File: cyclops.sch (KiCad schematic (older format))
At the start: 138 parts, among them J1 USB_mini_micro_B, K1 ESC, K10 KEYSW, K11 KEYSW, K12 KEYSW, K13 KEYSW, K14 backspace, K15 tab, K16 KEYSW, K17 KEYSW, K18 KEYSW, K19 KEYSW, K2 1, K20 KEYSW, K21 KEYSW, K22 KEYSW, K23 KEYSW, K24 KEYSW, K25 KEYSW, K26 KEYSW, K27 KEYSW, K28 Lock, K29 KEYSW, K3 KEYSW, K30 KEYSW, K31 KEYSW, K32 KEYSW, K33 KEYSW, K34 KEYSW, K35 KEYSW, K36 KEYSW, K37 KEYSW, K38 KEYSW, K39 KEYSW, K4 KEYSW, K40 KEYSW, K41 Shift, K42 KEYSW, K43 KEYSW, K44 KEYSW, K45 KEYSW, K46 KEYSW, K47 KEYSW, K48 KEYSW, K49 KEYSW, K5 KEYSW, K50 KEYSW, K51 KEYSW, K52 KEYSW, K53 Shift, K54 Ctrl, K55 alt, K56 opt, K57 space, K58 cmd, K59 alt, K6 KEYSW, K60 ctrl, K61 enter, K7 KEYSW, K8 KEYSW, K9 KEYSW, SW1 SW_Push, U1 ATMEGA32U2, X1 XTAL_GND

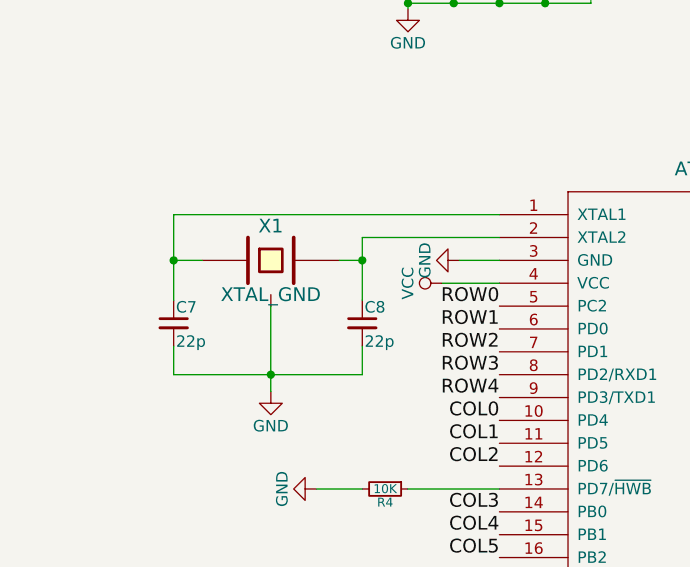
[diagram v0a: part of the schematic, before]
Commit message: PCB layout complete
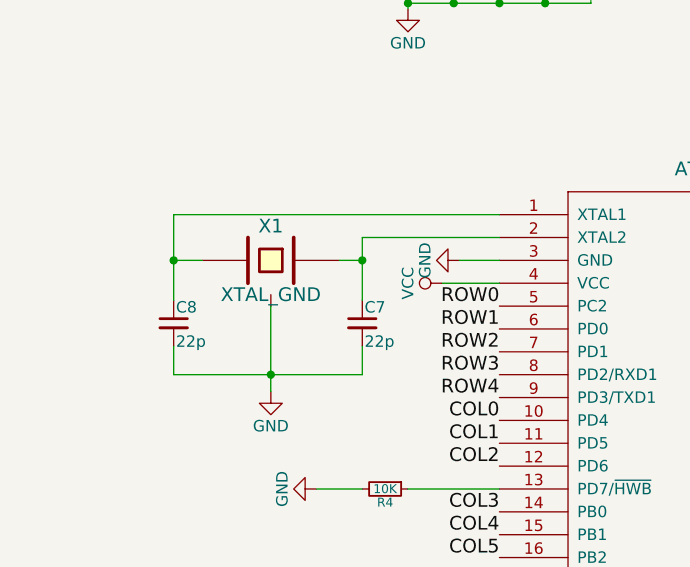
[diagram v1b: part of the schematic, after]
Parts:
- X1: footprint Crystals:Crystal_SMD_0603-4pin_6.0x3.5mm_HandSoldering -> Crystals:Crystal_SMD_SeikoEpson_FA238-4pin_3.2x2.5mm_HandSoldering
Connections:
- net at C7.1, X1.1: now also U1.2 (XTAL2); no longer U1.1 (XTAL1)
- net at C8.1, X1.2: now also U1.1 (XTAL1); no longer U1.2 (XTAL2)
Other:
- moved on the sheet: C7, C8
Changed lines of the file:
@@
 L C_Small C7
 U 1 1 5A32767B
-P 1425 3050
-F 0 "C7" H 1435 3120 50  0000 L CNN
-F 1 "22p" H 1435 2970 50  0000 L CNN
-F 2 "Capacitors_SMD:C_0805_HandSoldering" H 1425 3050 50  0001 C CNN
-F 3 "" H 1425 3050 50  0001 C CNN
-	1    1425 3050
+P 2250 3050
+F 0 "C7" H 2260 3120 50  0000 L CNN
+F 1 "22p" H 2260 2970 50  0000 L CNN
+F 2 "Capacitors_SMD:C_0805_HandSoldering" H 2250 3050 50  0001 C CNN
+F 3 "" H 2250 3050 50  0001 C CNN
+	1    2250 3050
 	1    0    0    -1
 $EndComp
@@
 L C_Small C8
 U 1 1 5A3276EA
-P 2250 3050
-F 0 "C8" H 2260 3120 50  0000 L CNN
-F 1 "22p" H 2260 2970 50  0000 L CNN
-F 2 "Capacitors_SMD:C_0805_HandSoldering" H 2250 3050 50  0001 C CNN
-F 3 "" H 2250 3050 50  0001 C CNN
-	1    2250 3050
+P 1425 3050
+F 0 "C8" H 1435 3120 50  0000 L CNN
+F 1 "22p" H 1435 2970 50  0000 L CNN
+F 2 "Capacitors_SMD:C_0805_HandSoldering" H 1425 3050 50  0001 C CNN
+F 3 "" H 1425 3050 50  0001 C CNN
+	1    1425 3050
 	1    0    0    -1
 $EndComp
@@
 F 0 "X1" H 1850 2925 60  0000 C CNN
 F 1 "XTAL_GND" H 1850 2625 60  0000 C CNN
-F 2 "Crystals:Crystal_SMD_0603-4pin_6.0x3.5mm_HandSoldering" H 1850 2775 60  0001 C CNN
+F 2 "Crystals:Crystal_SMD_SeikoEpson_FA238-4pin_3.2x2.5mm_HandSoldering" H 1850 2775 60  0001 C CNN
 F 3 "" H 1850 2775 60  0000 C CNN
 	1    1850 2775
-	1    0    0    -1
+	-1   0    0    -1
 $EndComp
 Wire Wire Line

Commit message: pcb complete
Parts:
- J1: footprint keyboard_parts:USB_miniB_hirose_5ST_hand -> keyboard_parts:USB_miniB_hirose_5S8
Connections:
- net COL0: now also U1.8 (PD2/RXD1); no longer U1.10 (PD4)
- net COL1: now also U1.7 (PD1); no longer U1.11 (PD5)
- net COL10: now also U1.20 (PB6); no longer U1.21 (PB7)
- net COL11: now also U1.21 (PB7); no longer U1.20 (PB6)
- net COL12: now also U1.23 (PC6); no longer U1.19 (PB5)
- net COL13: now also U1.22 (PC7); no longer U1.18 (PB4)
- net COL2: now also U1.9 (PD3/TXD1); no longer U1.12 (PD6)
- net COL3: now also U1.10 (PD4); no longer U1.14 (PB0)
- net COL4: now also U1.14 (PB0); no longer U1.15 (PB1)
- net COL5: now also U1.15 (PB1); no longer U1.16 (PB2)
- net COL6: now also U1.16 (PB2); no longer U1.26 (PC4)
- net COL7: now also U1.17 (PB3); no longer U1.25 (PC5)
- net COL8: now also U1.18 (PB4); no longer U1.23 (PC6)
- net COL9: now also U1.19 (PB5); no longer U1.22 (PC7)
- net GND: now also C6.2, J1.5 (GND), J1.6 (SHIELD), U1.28 (UGND)
- net ROW0: now also U1.6 (PD0); no longer U1.5 (PC2)
- net ROW1: now also D22.1 (K), U1.5 (PC2); no longer U1.6 (PD0)
- net ROW2: now also U1.11 (PD5); no longer U1.7 (PD1)
- net ROW3: now also U1.12 (PD6); no longer U1.8 (PD2/RXD1)
- net ROW4: now also U1.26 (PC4); no longer U1.9 (PD3/TXD1)
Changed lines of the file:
@@
 F 0 "J1" H 6225 2675 60  0000 C CNN
 F 1 "USB_mini_micro_B" H 6475 2975 60  0001 C CNN
-F 2 "keyboard_parts:USB_miniB_hirose_5ST_hand" H 6575 2725 60  0001 C CNN
+F 2 "keyboard_parts:USB_miniB_hirose_5S8" H 6575 2725 60  0001 C CNN
 F 3 "" H 6575 2725 60  0000 C CNN
 	1    6625 2725
@@
 	5250 2575 5250 2675
 Connection ~ 5250 2675
+Text Label 2850 3075 2    60   ~ 0
+ROW0
 Text Label 2850 2975 2    60   ~ 0
-ROW0
-Text Label 2850 3075 2    60   ~ 0
 ROW1
+Text Label 2850 3575 2    60   ~ 0
+ROW2
+Text Label 2850 3675 2    60   ~ 0
+ROW3
+Text Label 5000 3175 0    60   ~ 0
+ROW4
+Text Label 2850 3275 2    60   ~ 0
+COL0
 Text Label 2850 3175 2    60   ~ 0
-ROW2
-Text Label 2850 3275 2    60   ~ 0
-ROW3
+COL1
 Text Label 2850 3375 2    60   ~ 0
-ROW4
+COL2
 Text Label 2850 3475 2    60   ~ 0
-COL0
-Text Label 2850 3575 2    60   ~ 0
-COL1
-Text Label 2850 3675 2    60   ~ 0
-COL2
+COL3
 Text Label 2850 3875 2    60   ~ 0
-COL3
+COL4
 Text Label 2850 3975 2    60   ~ 0
-COL4
+COL5
 Text Label 2850 4075 2    60   ~ 0
-COL5
-Text Label 5000 3175 0    60   ~ 0
 COL6
-Text Label 5000 3275 0    60   ~ 0
+Text Label 5000 4075 0    60   ~ 0
 COL7
+Text Label 5000 3975 0    60   ~ 0
+COL8
+Text Label 5000 3875 0    60   ~ 0
+COL9
+Text Label 5000 3775 0    60   ~ 0
+COL10
+Text Label 5000 3675 0    60   ~ 0
+COL11
 Text Label 5000 3475 0    60   ~ 0
-COL8
+COL12
 Text Label 5000 3575 0    60   ~ 0
-COL9
-Text Label 5000 3675 0    60   ~ 0
-COL10
-Text Label 5000 3775 0    60   ~ 0
-COL11
-Text Label 5000 3875 0    60   ~ 0
-COL12
-Text Label 5000 3975 0    60   ~ 0
 COL13
-NoConn ~ 5000 4075
+NoConn ~ 5000 3275
+Connection ~ 9300 6650
+Connection ~ 4825 4325
+$Comp
+L GND #PWR010
+U 1 1 5A4D63E6
+P 6100 2975
+F 0 "#PWR010" H 6100 2725 50  0001 C CNN
+F 1 "GND" H 6100 2825 50  0000 C CNN
+F 2 "" H 6100 2975 50  0001 C CNN
+F 3 "" H 6100 2975 50  0001 C CNN
+	1    6100 2975
+	1    0    0    -1
+$EndComp
+Connection ~ 6100 2975
 $EndSCHEMATC

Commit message: pcb minor fixes
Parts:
- removed C3, C4: 0.1u, Capacitors_SMD:C_0805_HandSoldering, symbol C_Small
- renumbered C5 to C3, C6 to C4, C7 to C5, C8 to C6
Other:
- moved on the sheet: C3
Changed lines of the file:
@@
 $EndDescr
 $Comp
-L C_Small C7
+L C_Small C5
 U 1 1 5A32767B
 P 2250 3050
-F 0 "C7" H 2260 3120 50  0000 L CNN
+F 0 "C5" H 2260 3120 50  0000 L CNN
 F 1 "22p" H 2260 2970 50  0000 L CNN
 F 2 "Capacitors_SMD:C_0805_HandSoldering" H 2250 3050 50  0001 C CNN
@@
 $EndComp
 $Comp
-L C_Small C8
+L C_Small C6
 U 1 1 5A3276EA
 P 1425 3050
-F 0 "C8" H 1435 3120 50  0000 L CNN
+F 0 "C6" H 1435 3120 50  0000 L CNN
 F 1 "22p" H 1435 2970 50  0000 L CNN
 F 2 "Capacitors_SMD:C_0805_HandSoldering" H 1425 3050 50  0001 C CNN
@@
 Connection ~ 1850 3275
 $Comp
-L GND #PWR01
+L GND #PWR7
 U 1 1 5A32776A
 P 1850 3350
-F 0 "#PWR01" H 1850 3100 50  0001 C CNN
+F 0 "#PWR7" H 1850 3100 50  0001 C CNN
 F 1 "GND" H 1850 3200 50  0000 C CNN
 F 2 "" H 1850 3350 50  0001 C CNN
@@
 $Comp
 L C_Small C3
-U 1 1 5A328440
+U 1 1 5A3284C2
 P 2850 1500
 F 0 "C3" H 2860 1570 50  0000 L CNN
-F 1 "0.1u" H 2860 1420 50  0000 L CNN
+F 1 "4.7u" H 2860 1420 50  0000 L CNN
 F 2 "Capacitors_SMD:C_0805_HandSoldering" H 2850 1500 50  0001 C CNN
 F 3 "" H 2850 1500 50  0001 C CNN
@@
 $EndComp
 $Comp
-L C_Small C4
-U 1 1 5A32846F
-P 3050 1500
-F 0 "C4" H 3060 1570 50  0000 L CNN
-F 1 "0.1u" H 3060 1420 50  0000 L CNN
-F 2 "Capacitors_SMD:C_0805_HandSoldering" H 3050 1500 50  0001 C CNN
-F 3 "" H 3050 1500 50  0001 C CNN
-	1    3050 1500
-	1    0    0    -1
-$EndComp
-$Comp
-L C_Small C5
-U 1 1 5A3284C2
-P 3250 1500
-F 0 "C5" H 3260 1570 50  0000 L CNN
-F 1 "4.7u" H 3260 1420 50  0000 L CNN
-F 2 "Capacitors_SMD:C_0805_HandSoldering" H 3250 1500 50  0001 C CNN
-F 3 "" H 3250 1500 50  0001 C CNN
-	1    3250 1500
-	1    0    0    -1
-$EndComp
-$Comp
-L GND #PWR02
+L GND #PWR2
 U 1 1 5A328570
 P 2450 1675
-F 0 "#PWR02" H 2450 1425 50  0001 C CNN
+F 0 "#PWR2" H 2450 1425 50  0001 C CNN
 F 1 "GND" H 2450 1525 50  0000 C CNN
 F 2 "" H 2450 1675 50  0001 C CNN
@@
 $EndComp
 $Comp
-L VCC #PWR03
+L VCC #PWR1
 U 1 1 5A328596
 P 2450 1325
-F 0 "#PWR03" H 2450 1175 50  0001 C CNN
+F 0 "#PWR1" H 2450 1175 50  0001 C CNN
 F 1 "VCC" H 2450 1475 50  0000 C CNN
 F 2 "" H 2450 1325 50  0001 C CNN
@@
 Wire Wire Line
 	2450 1600 2450 1675
-Wire Wire Line
-	2450 1650 3250 1650
-Wire Wire Line
-	3250 1650 3250 1600
 Connection ~ 2450 1650
 Wire Wire Line
 	2450 1325 2450 1400
 Wire Wire Line
-	2450 1350 3250 1350
-Wire Wire Line
-	3250 1350 3250 1400
+	2450 1350 2850 1350
 Connection ~ 2450 1350
 Wire Wire Line
@@
 Connection ~ 2650 1350
 Wire Wire Line
-	2850 1400 2850 1350
-Connection ~ 2850 1350
+	2850 1350 2850 1400
 Wire Wire Line
 	2650 1600 2650 1650
@@
 Wire Wire Line
 	2850 1600 2850 1650
-Connection ~ 2850 1650
-Wire Wire Line
-	3050 1600 3050 1650
-Connection ~ 3050 1650
-Wire Wire Line
-	3050 1400 3050 1350
-Connection ~ 3050 1350
 $Comp
 L SW_Push SW1
@@
 	5000 3375 5450 3375
 $Comp
-L GND #PWR04
+L GND #PWR8
 U 1 1 5A328DC7
 P 5975 3375
-F 0 "#PWR04" H 5975 3125 50  0001 C CNN
+F 0 "#PWR8" H 5975 3125 50  0001 C CNN
 F 1 "GND" H 5975 3225 50  0000 C CNN
 F 2 "" H 5975 3375 50  0001 C CNN
@@
 $EndComp
 $Comp
-L VCC #PWR05
+L VCC #PWR9
 U 1 1 5A328DEF
 P 5900 3550
-F 0 "#PWR05" H 5900 3400 50  0001 C CNN
+F 0 "#PWR9" H 5900 3400 50  0001 C CNN
 F 1 "VCC" H 5900 3700 50  0000 C CNN
 F 2 "" H 5900 3550 50  0001 C CNN
@@
 	5975 3375 5850 3375
 $Comp
-L GND #PWR06
+L GND #PWR10
 U 1 1 5A328FCC
 P 2050 3775
-F 0 "#PWR06" H 2050 3525 50  0001 C CNN
+F 0 "#PWR10" H 2050 3525 50  0001 C CNN
 F 1 "GND" H 2050 3625 50  0000 C CNN
 F 2 "" H 2050 3775 50  0001 C CNN
@@
 	6200 2675 5000 2675
 $Comp
-L VCC #PWR07
+L VCC #PWR3
 U 1 1 5A329DCE
 P 6400 2550
-F 0 "#PWR07" H 6400 2400 50  0001 C CNN
+F 0 "#PWR3" H 6400 2400 50  0001 C CNN
 F 1 "VCC" H 6400 2700 50  0000 C CNN
 F 2 "" H 6400 2550 50  0001 C CNN
@@
 	5425 2975 5425 3075
 $Comp
-L C_Small C6
+L C_Small C4
 U 1 1 5A329E92
 P 5200 3075
-F 0 "C6" V 5224 3110 35  0000 L CNN
+F 0 "C4" V 5224 3110 35  0000 L CNN
 F 1 "1u" V 5224 3036 35  0000 R CNN
 F 2 "Capacitors_SMD:C_0805_HandSoldering" H 5200 3075 50  0001 C CNN
@@
 	6300 2675 6300 2775
 $Comp
-L VCC #PWR08
+L VCC #PWR5
 U 1 1 5A39CBC6
 P 2600 2875
-F 0 "#PWR08" H 2600 2725 50  0001 C CNN
+F 0 "#PWR5" H 2600 2725 50  0001 C CNN
 F 1 "VCC" H 2600 3025 50  0000 C CNN
 F 2 "" H 2600 2875 50  0001 C CNN
@@
 $EndComp
 $Comp
-L GND #PWR09
+L GND #PWR4
 U 1 1 5A39CCEE
 P 2675 2775
-F 0 "#PWR09" H 2675 2525 50  0001 C CNN
+F 0 "#PWR4" H 2675 2525 50  0001 C CNN
 F 1 "GND" H 2675 2625 50  0000 C CNN
 F 2 "" H 2675 2775 50  0001 C CNN
@@
 Connection ~ 4825 4325
 $Comp
-L GND #PWR010
+L GND #PWR6
 U 1 1 5A4D63E6
 P 6100 2975
-F 0 "#PWR010" H 6100 2725 50  0001 C CNN
+F 0 "#PWR6" H 6100 2725 50  0001 C CNN
 F 1 "GND" H 6100 2825 50  0000 C CNN
 F 2 "" H 6100 2975 50  0001 C CNN
@@
 $EndComp
 Connection ~ 6100 2975
+Wire Wire Line
+	2850 1650 2450 1650
 $EndSCHEMATC

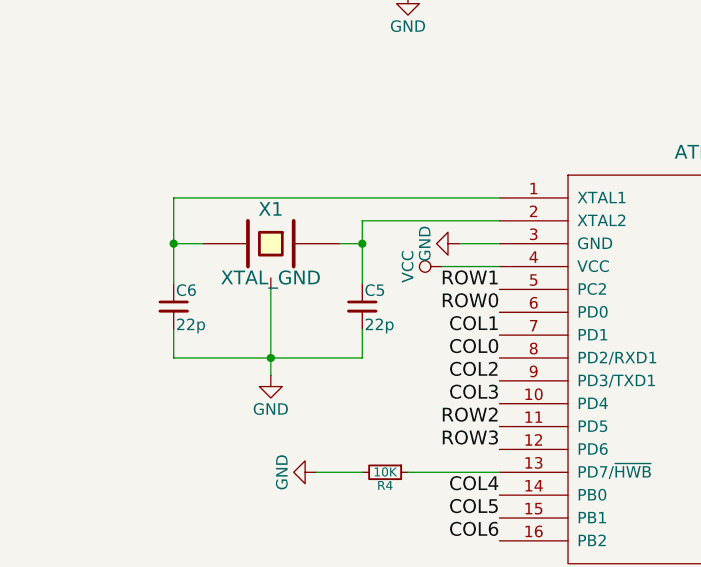
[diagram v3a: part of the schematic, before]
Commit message: Correct the crystal
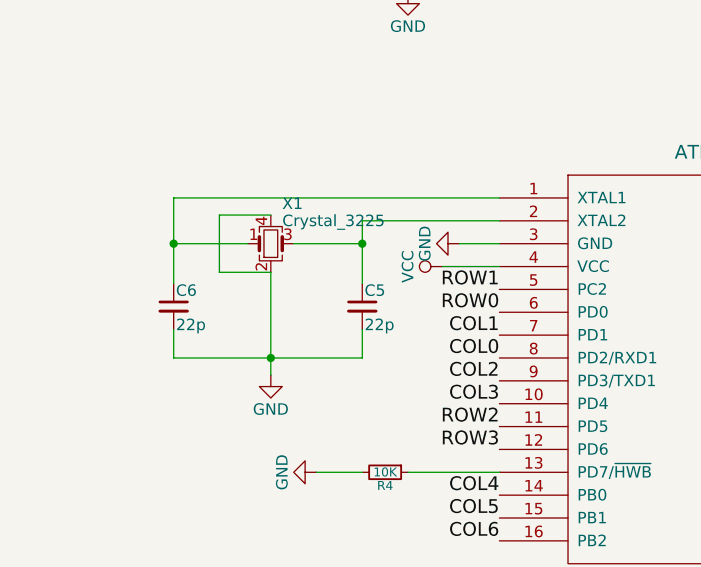
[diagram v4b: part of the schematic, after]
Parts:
- removed X1: XTAL_GND, Crystals:Crystal_SMD_SeikoEpson_FA238-4pin_3.2x2.5mm_HandSoldering, symbol XTAL_GND
- added X1: Crystal_3225, Crystals:Crystal_SMD_3225-4pin_3.2x2.5mm_HandSoldering, symbol Crystal_GND24_Small
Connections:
- net GND: now also X1.2, X1.4
- net at C5.1, U1.2 (XTAL2): now also X1.3
- net at C6.1, U1.1 (XTAL1): now also X1.1
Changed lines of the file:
@@
 LIBS:contrib
 LIBS:valves
-LIBS:cartel
-LIBS:keyboard_parts
-LIBS:mkl27z256vfm4
-LIBS:ws2812b
 LIBS:cyclops-cache
 EELAYER 25 0
@@
 $EndComp
 Wire Wire Line
-	2150 2775 2250 2775
+	1950 2775 2250 2775
 Wire Wire Line
 	2250 2675 2250 2950
@@
 	2250 3275 2250 3150
 Wire Wire Line
-	1850 2975 1850 3350
+	1850 2900 1850 3350
 Connection ~ 1850 3275
 $Comp
@@
 	1    0    0    -1
 $EndComp
-$Comp
-L XTAL_GND X1
-U 1 1 5A327837
-P 1850 2775
-F 0 "X1" H 1850 2925 60  0000 C CNN
-F 1 "XTAL_GND" H 1850 2625 60  0000 C CNN
-F 2 "Crystals:Crystal_SMD_SeikoEpson_FA238-4pin_3.2x2.5mm_HandSoldering" H 1850 2775 60  0001 C CNN
-F 3 "" H 1850 2775 60  0000 C CNN
-	1    1850 2775
-	-1   0    0    -1
-$EndComp
-Wire Wire Line
-	1425 2775 1550 2775
+Wire Wire Line
+	1425 2775 1750 2775
 $Comp
 L C_Small C1
@@
 Wire Wire Line
 	2850 1650 2450 1650
+$Comp
+L Crystal_GND24_Small X1
+U 1 1 5A4CE494
+P 1850 2775
+F 0 "X1" H 1900 2950 50  0000 L CNN
+F 1 "Crystal_3225" H 1900 2875 50  0000 L CNN
+F 2 "Crystals:Crystal_SMD_3225-4pin_3.2x2.5mm_HandSoldering" H 1850 2775 50  0001 C CNN
+F 3 "" H 1850 2775 50  0001 C CNN
+	1    1850 2775
+	1    0    0    -1
+$EndComp
+Wire Wire Line
+	1850 2650 1625 2650
+Wire Wire Line
+	1625 2650 1625 2900
+Wire Wire Line
+	1625 2900 1850 2900
 $EndSCHEMATC

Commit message: Revised design entirely
changed to 66-key
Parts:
- removed U1: ATMEGA32U2, keyboard_parts:QFP32, symbol ATMEGA32U2
- added C3, C4: 0.1u, Capacitor_SMD:C_0805_2012Metric_Pad1.15x1.40mm_HandSolder, symbol Device:C_Small
- added D62, D63, D64, D65, D66, D67: D, Diode_SMD:D_0805_2012Metric_Pad1.15x1.40mm_HandSolder, symbol Device:D
- added J2: Conn_02x03_Odd_Even, Pin_Headers:Pin_Header_Straight_2x03_Pitch2.54mm, symbol conn:Conn_02x03_Odd_Even
- added K62: backspace, MX_Alps_Hybrid:ALPS-1U, symbol keyboard_parts:KEYSW
- added K63: KEYSW, MX_Alps_Hybrid:ALPS-1U, symbol keyboard_parts:KEYSW
- added K64, K65, K66, K67: Shift, MX_Alps_Hybrid:ALPS-1U, symbol keyboard_parts:KEYSW
- added K64-2: Shift, MX_Alps_Hybrid:ALPS-2U, symbol keyboard_parts:KEYSW
- added U1: ATMEGA32U4, Package_QFP:TQFP-44_10x10mm_P0.8mm, symbol keyboard_parts:ATMEGA32U4
- C1, C2: footprint Capacitors_SMD:C_0805_HandSoldering -> Capacitor_SMD:C_0805_2012Metric_Pad1.15x1.40mm_HandSolder; symbol C_Small -> Device:C_Small
- C5: renamed from C3; footprint Capacitors_SMD:C_0805_HandSoldering -> Capacitor_SMD:C_0805_2012Metric_Pad1.15x1.40mm_HandSolder; symbol C_Small -> Device:C_Small
- C6: renamed from C5; footprint Capacitors_SMD:C_0805_HandSoldering -> Capacitor_SMD:C_0805_2012Metric_Pad1.15x1.40mm_HandSolder; symbol C_Small -> Device:C_Small
- C7: renamed from C6; footprint Capacitors_SMD:C_0805_HandSoldering -> Capacitor_SMD:C_0805_2012Metric_Pad1.15x1.40mm_HandSolder; symbol C_Small -> Device:C_Small
- C8: renamed from C4; footprint Capacitors_SMD:C_0805_HandSoldering -> Capacitor_SMD:C_0805_2012Metric_Pad1.15x1.40mm_HandSolder; symbol C_Small -> Device:C_Small
- D1, D10, D11, D12, D13, D14, D15, D16, D17, D18, D19, D2, D20, D21, D22, D23, D24, D25, D26, D27, D28, D29, D3, D30, D31, D32, D33, D34, D35, D36, D37, D38, D39, D4, D40, D41, D42, D43, D44, D45, D46, D47, D48, D49, D5, D50, D51, D52, D53, D54, D55, D56, D57, D58, D59, D6, D60, D61, D7, D8, D9: footprint Diodes_SMD:D_SOD-323_HandSoldering -> Diode_SMD:D_0805_2012Metric_Pad1.15x1.40mm_HandSolder; symbol D -> Device:D
- J1: footprint keyboard_parts:USB_miniB_hirose_5S8 -> Connector_USB:U-M-M5DD-W-1; symbol USB_mini_micro_B -> keyboard_parts:USB_mini_micro_B
- K1, K10, K11, K12, K13, K14, K15, K16, K17, K18, K19, K2, K20, K21, K22, K23, K24, K25, K26, K27, K28, K29, K3, K30, K31, K32, K33, K34, K35, K36, K37, K38, K39, K4, K40, K41, K42, K43, K44, K45, K46, K47, K48, K49, K5, K50, K51, K52, K54, K55, K56, K57, K58, K59, K6, K61, K7, K8, K9: symbol KEYSW -> keyboard_parts:KEYSW
- K53: footprint MX_Alps_Hybrid:ALPS-2.5U -> MX_Alps_Hybrid:ALPS-1U; symbol KEYSW -> keyboard_parts:KEYSW
- K60: footprint MX_Alps_Hybrid:ALPS-1.5U -> MX_Alps_Hybrid:ALPS-1U; symbol KEYSW -> keyboard_parts:KEYSW
- R1, R2: symbol R -> Device:R
- R3, R4: symbol R_Small -> Device:R_Small
- SW1: symbol SW_Push -> switches:SW_Push
- X1: symbol Crystal_GND24_Small -> Device:Crystal_GND24_Small
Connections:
- net labels added: COL14, MISO, MOSI, RESET, SCK
- wire segments 315 -> 496
- no-connect marks 2 -> 7
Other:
- moved on the sheet: C1, C2, C5, C6, C7, C8, D1, D10, D11, D12, D13, D14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

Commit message: Updated to Rev. 3
corrected some issues with footprints

adjusted some traces to be less close to easily damaged parts

added silkscreen details for the board

adjusted iso footprint

changed some footrprints to updated ones

updated gerbers

added readme
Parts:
- X1: footprint Crystals:Crystal_SMD_3225-4pin_3.2x2.5mm_HandSoldering -> Crystal:Crystal_SMD_3225-4Pin_3.2x2.5mm
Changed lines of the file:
@@
 F 0 "X1" H 7150 3900 50  0000 L CNN
 F 1 "Crystal_3225" H 7150 3825 50  0000 L CNN
-F 2 "Crystals:Crystal_SMD_3225-4pin_3.2x2.5mm_HandSoldering" H 7100 3725 50  0001 C CNN
+F 2 "Crystal:Crystal_SMD_3225-4Pin_3.2x2.5mm" H 7100 3725 50  0001 C CNN
 F 3 "" H 7100 3725 50  0001 C CNN
 	1    7100 3725
